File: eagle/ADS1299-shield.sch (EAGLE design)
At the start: 124 parts, among them IC1 ADS1299IPAG, IC2 TPS72325DBVT, IC3 TPS73225DBVT, IC5 24AA256UID, IC6 TPS604XXDBV, IC7 OPA376DBV, IC8 OPA376DBV, J8 Electrode Connector, U2 TXB0108PWR, U3 TXB0108PWR

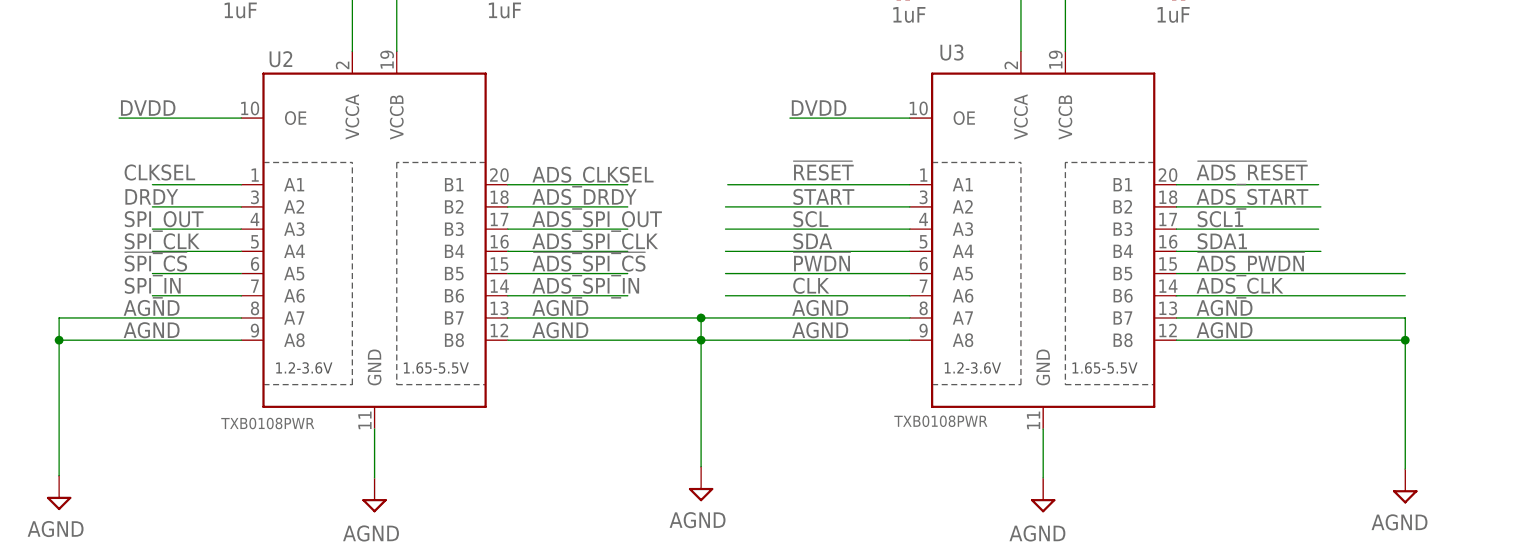
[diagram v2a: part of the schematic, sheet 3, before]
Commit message: fully routed ADS1299 CLK signal to connector pins
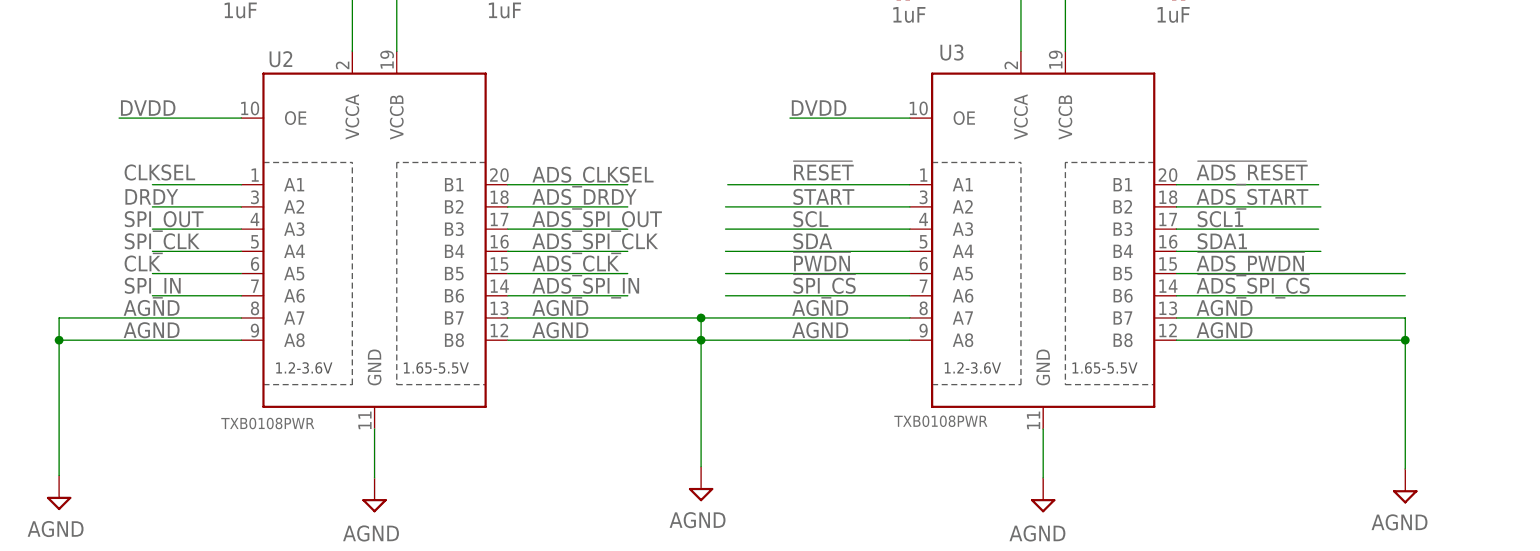
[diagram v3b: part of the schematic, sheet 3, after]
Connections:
- net !ADS_SPI_CS: now also U3.B6; no longer U2.B5
- net !SPI_CS: now also U3.A6; no longer U2.A5
- net ADS_CLK: now also U2.B5; no longer U3.B6
- net CLK: now also U2.A5; no longer U3.A6
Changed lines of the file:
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@@
 <net name="CLK" class="0">
 <segment>
-<pinref part="U3" gate="G$1" pin="A6"/>
-<wire x1="137.414" y1="202.692" x2="116.332" y2="202.692" width="0.1524" layer="91"/>
-<label x="123.952" y="202.946" size="1.778" layer="95"/>
+<pinref part="U2" gate="G$1" pin="A5"/>
+<wire x1="60.96" y1="205.232" x2="50.8" y2="205.232" width="0.1524" layer="91"/>
+<label x="47.498" y="205.486" size="1.778" layer="95"/>
 </segment>
 </net>
@@
 <net name="ADS_SPI_IN" class="0">
 <segment>
-<pinref part="U2" gate="G$1" pin="B6"/>
-<wire x1="91.44" y1="202.692" x2="105.156" y2="202.692" width="0.1524" layer="91"/>
-<label x="94.234" y="202.946" size="1.778" layer="95"/>
-</segment>
-<segment>
 <wire x1="194.31" y1="32.004" x2="185.928" y2="32.004" width="0.1524" layer="91"/>
 <label x="177.8" y="32.512" size="1.27" layer="95"/>
@@
 <pinref part="JP2" gate="A" pin="19"/>
 </segment>
+<segment>
+<pinref part="U2" gate="G$1" pin="B6"/>
+<wire x1="91.44" y1="202.692" x2="105.156" y2="202.692" width="0.1524" layer="91"/>
+<label x="94.234" y="202.946" size="1.778" layer="95"/>
+</segment>
 </net>
 <net name="ADS_SPI_OUT" class="0">
@@
 </segment>
 <segment>
-<pinref part="U3" gate="G$1" pin="B6"/>
-<wire x1="167.894" y1="202.692" x2="194.056" y2="202.692" width="0.1524" layer="91"/>
-<label x="170.18" y="202.946" size="1.778" layer="95"/>
+<pinref part="U2" gate="G$1" pin="B5"/>
+<wire x1="91.44" y1="205.232" x2="105.156" y2="205.232" width="0.1524" layer="91"/>
+<label x="94.234" y="205.486" size="1.778" layer="95"/>
 </segment>
 </net>
@@
 </segment>
 <segment>
-<pinref part="U2" gate="G$1" pin="B5"/>
-<wire x1="91.44" y1="205.232" x2="105.156" y2="205.232" width="0.1524" layer="91"/>
-<label x="94.234" y="205.486" size="1.778" layer="95"/>
+<pinref part="U3" gate="G$1" pin="B6"/>
+<wire x1="167.894" y1="202.692" x2="194.056" y2="202.692" width="0.1524" layer="91"/>
+<label x="170.18" y="202.946" size="1.778" layer="95"/>
 </segment>
 </net>
@@
 </segment>
 </net>
-<net name="!SPI_CS" class="0">
-<segment>
-<pinref part="U2" gate="G$1" pin="A5"/>
-<wire x1="60.96" y1="205.232" x2="50.8" y2="205.232" width="0.1524" layer="91"/>
-<label x="47.498" y="205.486" size="1.778" layer="95"/>
-</segment>
-</net>
 <net name="SPI_IN" class="0">
 <segment>
@@
 </segment>
 </net>
+<net name="!SPI_CS" class="0">
+<segment>
+<pinref part="U3" gate="G$1" pin="A6"/>
+<wire x1="137.414" y1="202.692" x2="116.332" y2="202.692" width="0.1524" layer="91"/>
+<label x="123.952" y="202.946" size="1.778" layer="95"/>
+</segment>
+</net>

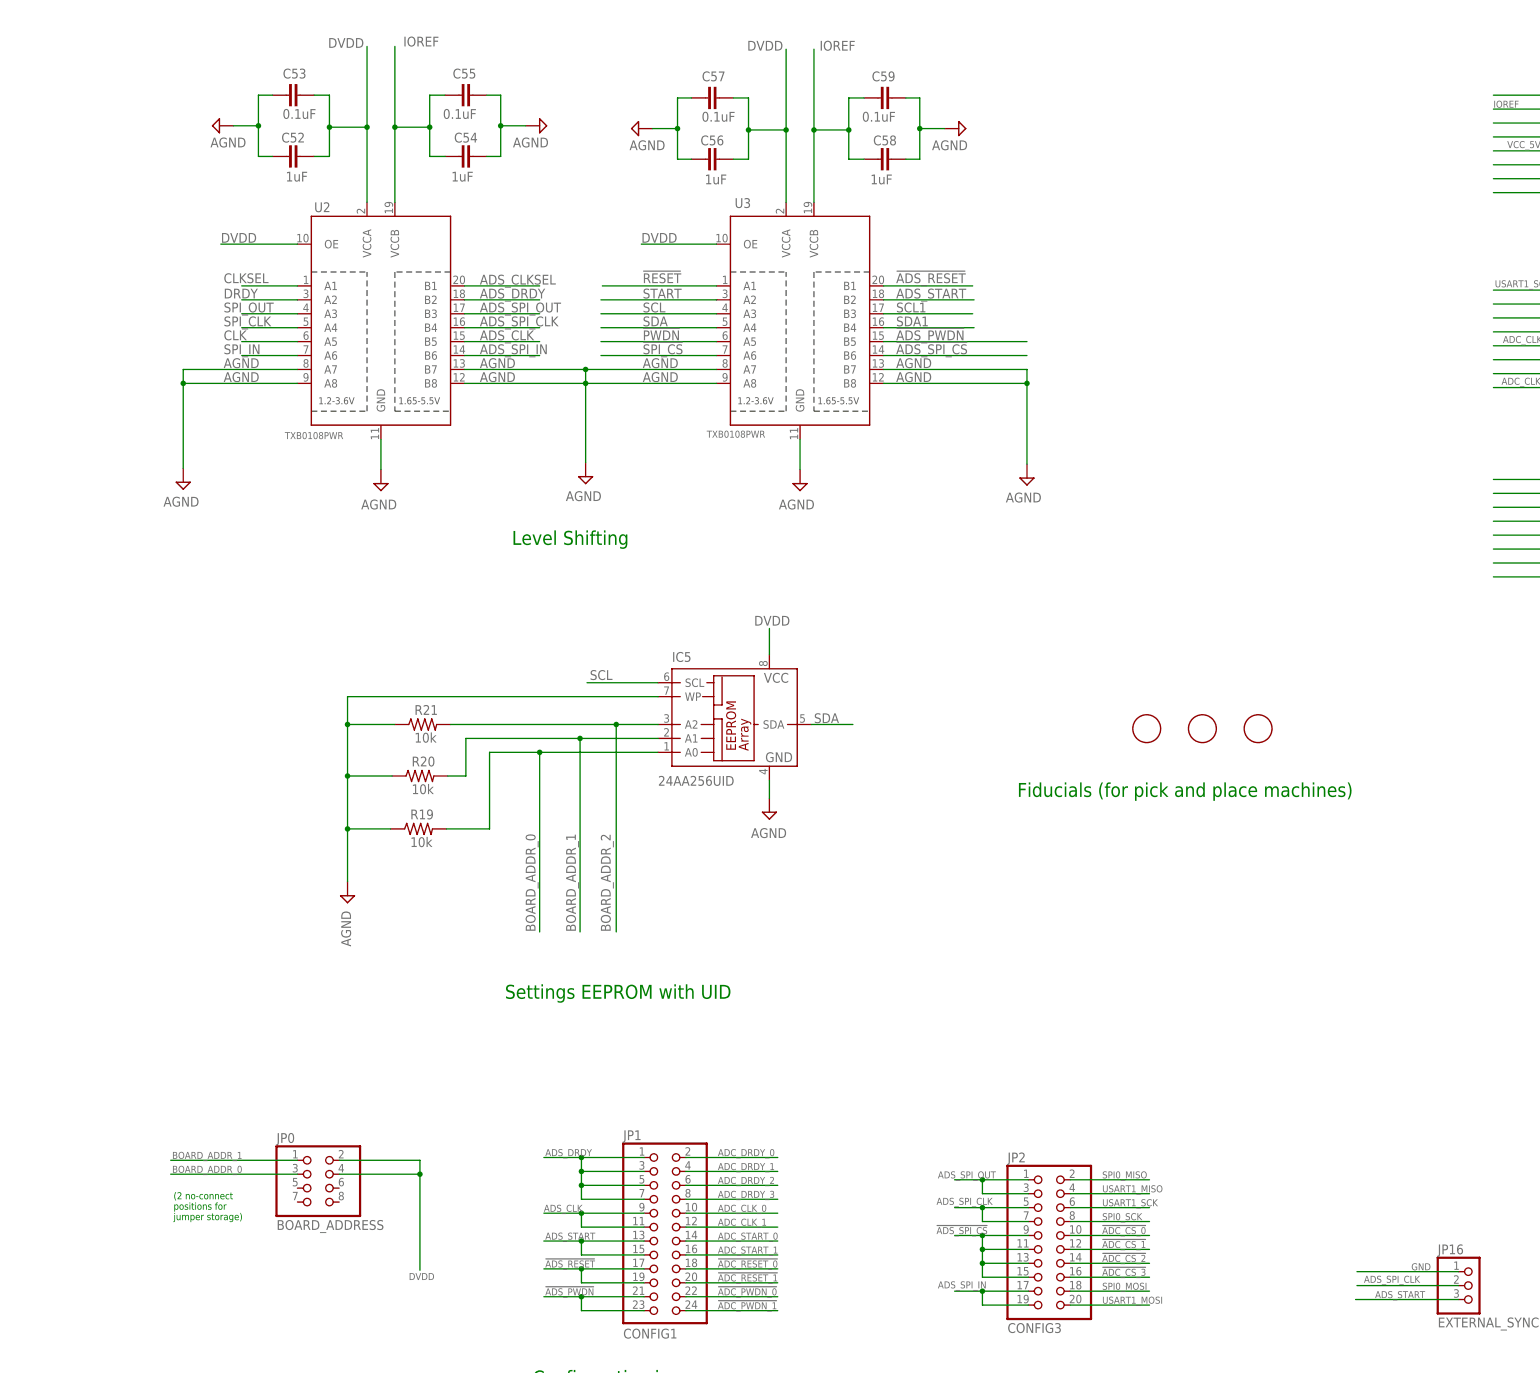
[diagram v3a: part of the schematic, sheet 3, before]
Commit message: routed more AGND and AVDD signals to use AVDD and AGND layers
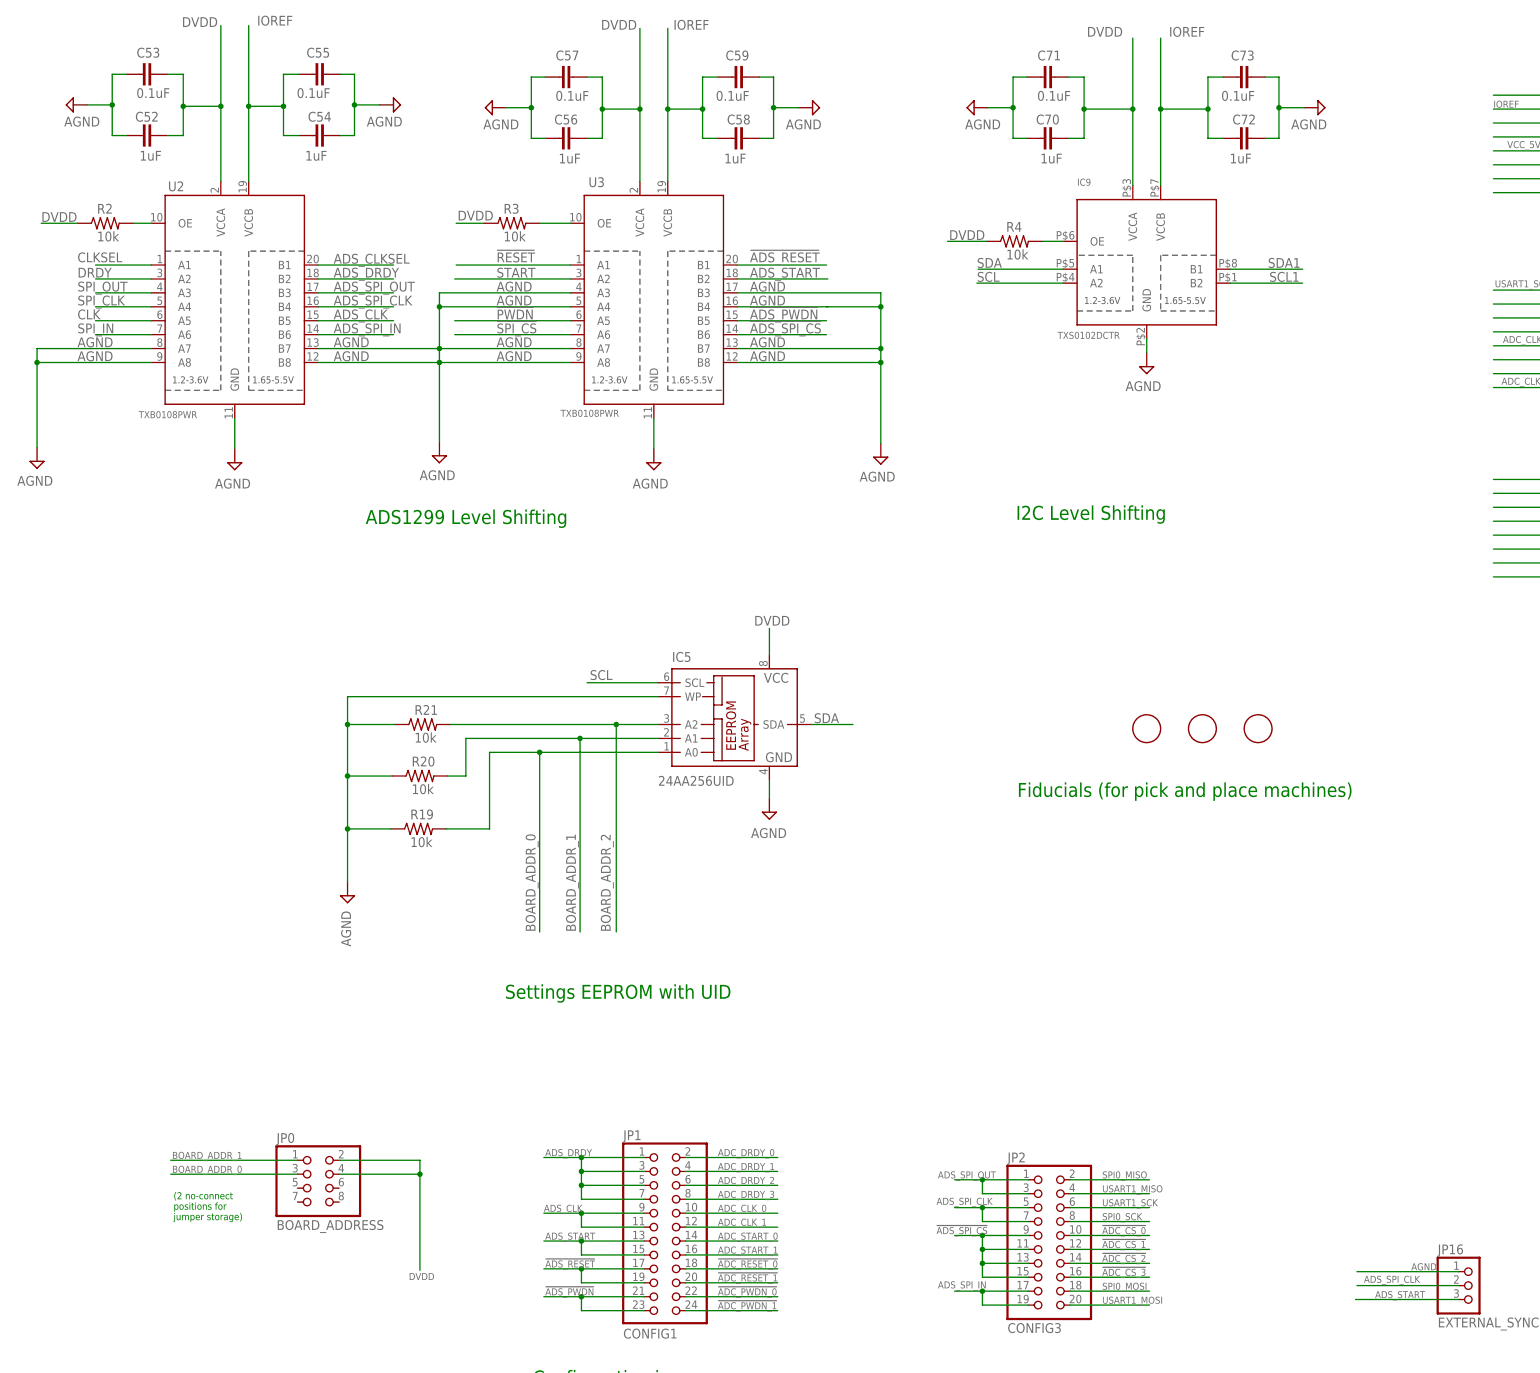
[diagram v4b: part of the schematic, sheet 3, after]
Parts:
- added C70, C72: 1uF, SparkFun-Passives:CAP0603-CAP
- added C71, C73: 0.1uF, SparkFun-Passives:CAP0603-CAP
- added IC9: TXS0102DCTR, adafruit:TXS0102
- added R2, R3, R4: 10k, SparkFun-Passives:RESISTOR0603-RES
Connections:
- removed net GND: C7.2, C8.2, JP16.1
- new net N$37: IC9.OE, R4.2
- new net N$561: R2.2, U2.OE
- new net N$562: R3.2, U3.OE
- net AGND: now also C70.1, C71.1, C72.1, C73.1, IC9.GND, JP16.1, U3.A3, U3.A4, U3.B3, U3.B4
- net AVSS: now also C7.2, C8.2
- net DVDD: now also C70.2, C71.2, IC9.VCCA, R2.1, R3.1, R4.1; no longer U2.OE, U3.OE
- net IOREF: now also C72.2, C73.2, IC9.VCCB
- net SCL: now also IC9.A2; no longer U3.A3
- net SCL1: now also IC9.B2; no longer U3.B3
- net SDA: now also IC9.A1; no longer U3.A4
- net SDA1: now also IC9.B1; no longer U3.B4
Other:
- note added: "ADS1299 Level Shifting"
- note added: "I2C Level Shifting"
- note removed: "Level Shifting"
- moved on the sheet: C52, C53, C54, C55, C56, C57, C58, C59, U2, U3

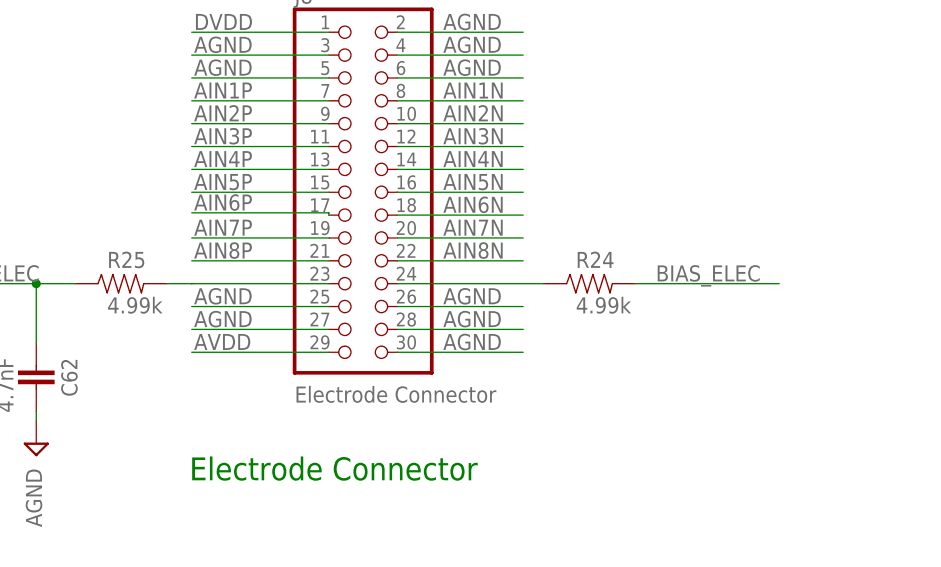
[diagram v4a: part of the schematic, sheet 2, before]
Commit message: routed JST connector signals - ADS_CLK, ADS_START, AGND
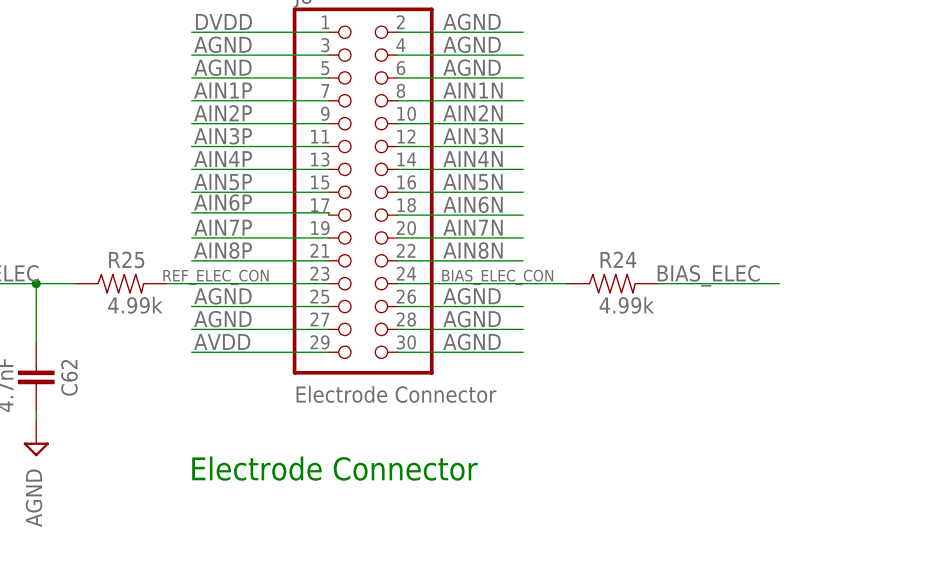
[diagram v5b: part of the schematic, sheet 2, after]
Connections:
- net N$105 renamed REF_ELEC_CON
- net N$106 renamed BIAS_ELEC_CON
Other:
- moved on the sheet: R24
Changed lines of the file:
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@@
 <attribute name="VALUE" x="344.424" y="206.248" size="1.778" layer="96" rot="R180"/>
 </instance>
-<instance part="R24" gate="G$1" x="108.966" y="57.15" smashed="yes">
-<attribute name="NAME" x="107.442" y="58.9026" size="1.778" layer="95"/>
-<attribute name="VALUE" x="107.442" y="53.848" size="1.778" layer="96"/>
+<instance part="R24" gate="G$1" x="111.506" y="57.15" smashed="yes">
+<attribute name="NAME" x="109.982" y="58.9026" size="1.778" layer="95"/>
+<attribute name="VALUE" x="109.982" y="53.848" size="1.778" layer="96"/>
 </instance>
 <instance part="R25" gate="G$1" x="56.896" y="57.15" smashed="yes">
@@
 </segment>
 </net>
-<net name="N$105" class="0">
+<net name="REF_ELEC_CON" class="0">
 <segment>
 <pinref part="J8" gate="A" pin="23"/>
-<wire x1="80.01" y1="57.15" x2="65.024" y2="57.15" width="0.1524" layer="91"/>
+<wire x1="80.01" y1="57.15" x2="61.976" y2="57.15" width="0.1524" layer="91"/>
 <pinref part="R25" gate="G$1" pin="2"/>
-<wire x1="65.024" y1="57.15" x2="64.77" y2="57.15" width="0.1524" layer="91"/>
-<wire x1="61.976" y1="57.15" x2="64.77" y2="57.15" width="0.1524" layer="91"/>
+<label x="61.468" y="57.404" size="1.27" layer="95"/>
 </segment>
 </net>
@@
 <segment>
 <pinref part="R24" gate="G$1" pin="2"/>
-<wire x1="114.046" y1="57.15" x2="130.048" y2="57.15" width="0.1524" layer="91"/>
+<wire x1="116.586" y1="57.15" x2="130.048" y2="57.15" width="0.1524" layer="91"/>
 <label x="116.332" y="57.404" size="1.778" layer="95"/>
 </segment>
@@
 </segment>
 </net>
-<net name="N$106" class="0">
+<net name="BIAS_ELEC_CON" class="0">
 <segment>
 <pinref part="J8" gate="A" pin="24"/>
 <pinref part="R24" gate="G$1" pin="1"/>
-<wire x1="87.63" y1="57.15" x2="103.886" y2="57.15" width="0.1524" layer="91"/>
-</segment>
-</net>
+<wire x1="87.63" y1="57.15" x2="106.426" y2="57.15" width="0.1524" layer="91"/>
+<label x="92.456" y="57.404" size="1.27" layer="95"/>
+</segment>
+</net>

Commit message: configuration jumper section completely routed
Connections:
- new net N$570: JP14.5
- new net N$571: JP11.1
- new net N$572: JP11.2
- net VCC_5V: no longer JP11.1, JP11.2, JP14.5
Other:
- note added: "Pins not labeled are not connected (NC)"
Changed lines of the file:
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@@
 <text x="353.314" y="171.704" size="1.524" layer="91">RX2</text>
 <text x="192.024" y="172.72" size="2.54" layer="91">I2C Level Shifting</text>
+<text x="304.8" y="264.16" size="1.778" layer="91">Pins not labeled are not connected (NC)</text>
 </plain>
 <instances>
@@
 <net name="VCC_5V" class="0">
 <segment>
-<pinref part="JP14" gate="A" pin="5"/>
-<wire x1="302.26" y1="240.03" x2="279.146" y2="240.03" width="0.1524" layer="91"/>
-<label x="287.782" y="241.808" size="1.27" layer="95" rot="R180"/>
-</segment>
-<segment>
 <pinref part="JP15" gate="A" pin="2"/>
 <wire x1="337.82" y1="203.2" x2="337.82" y2="189.738" width="0.1524" layer="91"/>
 <label x="337.312" y="191.516" size="1.27" layer="95" rot="R90"/>
-</segment>
-<segment>
-<pinref part="JP11" gate="A" pin="2"/>
-<wire x1="355.346" y1="117.348" x2="355.346" y2="105.156" width="0.1524" layer="91"/>
-<label x="355.092" y="104.902" size="1.27" layer="95" rot="R90"/>
-</segment>
-<segment>
-<pinref part="JP11" gate="A" pin="1"/>
-<wire x1="355.346" y1="124.968" x2="355.346" y2="137.16" width="0.1524" layer="91"/>
-<label x="354.838" y="129.286" size="1.27" layer="95" rot="R90"/>
 </segment>
 </net>
@@
 </segment>
 </net>
+<net name="N$570" class="0">
+<segment>
+<pinref part="JP14" gate="A" pin="5"/>
+<wire x1="302.26" y1="240.03" x2="279.146" y2="240.03" width="0.1524" layer="91"/>
+</segment>
+</net>
+<net name="N$571" class="0">
+<segment>
+<pinref part="JP11" gate="A" pin="1"/>
+<wire x1="355.346" y1="124.968" x2="355.346" y2="137.16" width="0.1524" layer="91"/>
+</segment>
+</net>
+<net name="N$572" class="0">
+<segment>
+<pinref part="JP11" gate="A" pin="2"/>
+<wire x1="355.346" y1="117.348" x2="355.346" y2="105.156" width="0.1524" layer="91"/>
+</segment>
+</net>
